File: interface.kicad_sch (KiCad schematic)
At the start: 6 parts, among them J10 RJ12, J11 Conn_01x06_Female, J8 Conn_01x06_Male, J9 RJ12, U5 MAX485E

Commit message: redone the switch connectors to accomodate a current sense print. Rearranged parts and updated silk texts to be 50% of their original size
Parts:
- renumbered C8 to C601, J8 to J601, J9 to J602, J10 to J603, J11 to J604, U5 to U601
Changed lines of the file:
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@@
   (symbol (lib_id "power:+12V") (at 143.51 50.8 0) (unit 1)
     (in_bom yes) (on_board yes) (fields_autoplaced)
-    (property "Reference" "#PWR0134" (id 0) (at 143.51 54.61 0)
+    (property "Reference" "#PWR0603" (id 0) (at 143.51 54.61 0)
       (effects (font (size 1.27 1.27)) hide)
     )
@@
   (symbol (lib_id "Connector:Conn_01x06_Female") (at 135.89 116.84 0) (mirror x) (unit 1)
     (in_bom yes) (on_board yes)
-    (property "Reference" "J11" (id 0) (at 136.6012 116.4785 0)
+    (property "Reference" "J604" (id 0) (at 136.6012 116.4785 0)
       (effects (font (size 1.27 1.27)) (justify left))
     )
@@
   (symbol (lib_id "power:GND") (at 143.51 93.98 0) (unit 1)
     (in_bom yes) (on_board yes) (fields_autoplaced)
-    (property "Reference" "#PWR0138" (id 0) (at 143.51 100.33 0)
+    (property "Reference" "#PWR0606" (id 0) (at 143.51 100.33 0)
       (effects (font (size 1.27 1.27)) hide)
     )
@@
   (symbol (lib_id "Connector:RJ12") (at 130.81 86.36 0) (unit 1)
     (in_bom yes) (on_board yes) (fields_autoplaced)
-    (property "Reference" "J10" (id 0) (at 130.81 72.5002 0))
+    (property "Reference" "J603" (id 0) (at 130.81 72.5002 0))
     (property "Value" "RJ12" (id 1) (at 130.81 75.0371 0))
     (property "Footprint" "Connector_RJ:RJ12_Amphenol_54601" (id 2) (at 130.81 85.725 90)
@@
   (symbol (lib_id "power:+12V") (at 128.27 107.95 0) (unit 1)
     (in_bom yes) (on_board yes) (fields_autoplaced)
-    (property "Reference" "#PWR0137" (id 0) (at 128.27 111.76 0)
+    (property "Reference" "#PWR0601" (id 0) (at 128.27 111.76 0)
       (effects (font (size 1.27 1.27)) hide)
     )
@@
   (symbol (lib_id "power:GND") (at 167.64 116.84 0) (unit 1)
     (in_bom yes) (on_board yes) (fields_autoplaced)
-    (property "Reference" "#PWR0140" (id 0) (at 167.64 123.19 0)
+    (property "Reference" "#PWR0610" (id 0) (at 167.64 123.19 0)
       (effects (font (size 1.27 1.27)) hide)
     )
@@
   (symbol (lib_id "Connector:Conn_01x06_Male") (at 120.65 116.84 0) (mirror x) (unit 1)
     (in_bom yes) (on_board yes)
-    (property "Reference" "J8" (id 0) (at 121.285 125.9627 0))
+    (property "Reference" "J601" (id 0) (at 121.285 125.9627 0))
     (property "Value" "Conn_01x06_Male" (id 1) (at 146.05 114.3 0))
     (property "Footprint" "Connector_PinHeader_2.54mm:PinHeader_1x06_P2.54mm_Horizontal" (id 2) (at 120.65 116.84 0)
@@
   (symbol (lib_id "Interface_UART:MAX485E") (at 162.56 67.31 0) (mirror y) (unit 1)
     (in_bom yes) (on_board yes) (fields_autoplaced)
-    (property "Reference" "U5" (id 0) (at 163.0806 53.4502 0)
+    (property "Reference" "U601" (id 0) (at 163.0806 53.4502 0)
       (effects (font (size 1.27 1.27)) (justify right))
     )
@@
   (symbol (lib_id "power:GND") (at 143.51 67.31 0) (unit 1)
     (in_bom yes) (on_board yes) (fields_autoplaced)
-    (property "Reference" "#PWR0136" (id 0) (at 143.51 73.66 0)
+    (property "Reference" "#PWR0604" (id 0) (at 143.51 73.66 0)
       (effects (font (size 1.27 1.27)) hide)
     )
@@
   (symbol (lib_id "power:+5V") (at 167.64 104.14 0) (unit 1)
     (in_bom yes) (on_board yes) (fields_autoplaced)
-    (property "Reference" "#PWR0142" (id 0) (at 167.64 107.95 0)
+    (property "Reference" "#PWR0609" (id 0) (at 167.64 107.95 0)
       (effects (font (size 1.27 1.27)) hide)
     )
@@
   (symbol (lib_id "Device:C") (at 167.64 110.49 0) (unit 1)
     (in_bom yes) (on_board yes) (fields_autoplaced)
-    (property "Reference" "C8" (id 0) (at 170.561 109.6553 0)
+    (property "Reference" "C601" (id 0) (at 170.561 109.6553 0)
       (effects (font (size 1.27 1.27)) (justify left))
     )
@@
   (symbol (lib_id "power:+5V") (at 162.56 50.8 0) (unit 1)
     (in_bom yes) (on_board yes) (fields_autoplaced)
-    (property "Reference" "#PWR0133" (id 0) (at 162.56 54.61 0)
+    (property "Reference" "#PWR0607" (id 0) (at 162.56 54.61 0)
       (effects (font (size 1.27 1.27)) hide)
     )
@@
   (symbol (lib_id "power:+12V") (at 143.51 77.47 0) (unit 1)
     (in_bom yes) (on_board yes) (fields_autoplaced)
-    (property "Reference" "#PWR0135" (id 0) (at 143.51 81.28 0)
+    (property "Reference" "#PWR0605" (id 0) (at 143.51 81.28 0)
       (effects (font (size 1.27 1.27)) hide)
     )
@@
   (symbol (lib_id "power:GND") (at 162.56 85.09 0) (unit 1)
     (in_bom yes) (on_board yes) (fields_autoplaced)
-    (property "Reference" "#PWR0143" (id 0) (at 162.56 91.44 0)
+    (property "Reference" "#PWR0608" (id 0) (at 162.56 91.44 0)
       (effects (font (size 1.27 1.27)) hide)
     )
@@
   (symbol (lib_id "power:GND") (at 128.27 123.19 0) (unit 1)
     (in_bom yes) (on_board yes) (fields_autoplaced)
-    (property "Reference" "#PWR0139" (id 0) (at 128.27 129.54 0)
+    (property "Reference" "#PWR0602" (id 0) (at 128.27 129.54 0)
       (effects (font (size 1.27 1.27)) hide)
     )
@@
   (symbol (lib_id "Connector:RJ12") (at 130.81 59.69 0) (unit 1)
     (in_bom yes) (on_board yes) (fields_autoplaced)
-    (property "Reference" "J9" (id 0) (at 130.81 45.8302 0))
+    (property "Reference" "J602" (id 0) (at 130.81 45.8302 0))
     (property "Value" "RJ12" (id 1) (at 130.81 48.3671 0))
     (property "Footprint" "Connector_RJ:RJ12_Amphenol_54601" (id 2) (at 130.81 59.055 90)

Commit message: I have a problem that I lose the links between symbols and footprints. I want to add a spst switch to connect the bus' voltage to the main power
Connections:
- net +12V renamed +12VA
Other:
- moved on the sheet: C601
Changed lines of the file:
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@@
     (stroke (width 0) (type default) (color 0 0 0 0))
   )
-  (wire (pts (xy 167.64 114.3) (xy 167.64 116.84))
+  (wire (pts (xy 190.5 72.39) (xy 190.5 74.93))
     (stroke (width 0) (type default) (color 0 0 0 0))
   )
@@
     (stroke (width 0) (type default) (color 0 0 0 0))
   )
-  (wire (pts (xy 167.64 104.14) (xy 167.64 106.68))
+  (wire (pts (xy 190.5 62.23) (xy 190.5 64.77))
     (stroke (width 0) (type default) (color 0 0 0 0))
   )
@@
     )
   )
-  (symbol (lib_id "power:+12V") (at 143.51 50.8 0) (unit 1)
-    (in_bom yes) (on_board yes) (fields_autoplaced)
-    (property "Reference" "#PWR0603" (id 0) (at 143.51 54.61 0)
-      (effects (font (size 1.27 1.27)) hide)
-    )
-    (property "Value" "+12V" (id 1) (at 143.51 47.1955 0))
-    (property "Footprint" "" (id 2) (at 143.51 50.8 0)
-      (effects (font (size 1.27 1.27)) hide)
-    )
-    (property "Datasheet" "" (id 3) (at 143.51 50.8 0)
+  (symbol (lib_id "power:+12VA") (at 128.27 107.95 0) (unit 1)
+    (in_bom yes) (on_board yes) (fields_autoplaced)
+    (property "Reference" "#PWR0601" (id 0) (at 128.27 111.76 0)
+      (effects (font (size 1.27 1.27)) hide)
+    )
+    (property "Value" "+12VA" (id 1) (at 128.27 104.3742 0))
+    (property "Footprint" "" (id 2) (at 128.27 107.95 0)
+      (effects (font (size 1.27 1.27)) hide)
+    )
+    (property "Datasheet" "" (id 3) (at 128.27 107.95 0)
       (effects (font (size 1.27 1.27)) hide)
     )
@@
     (pin "6")
   )
-  (symbol (lib_id "power:+12V") (at 128.27 107.95 0) (unit 1)
-    (in_bom yes) (on_board yes) (fields_autoplaced)
-    (property "Reference" "#PWR0601" (id 0) (at 128.27 111.76 0)
-      (effects (font (size 1.27 1.27)) hide)
-    )
-    (property "Value" "+12V" (id 1) (at 128.27 104.3742 0))
-    (property "Footprint" "" (id 2) (at 128.27 107.95 0)
-      (effects (font (size 1.27 1.27)) hide)
-    )
-    (property "Datasheet" "" (id 3) (at 128.27 107.95 0)
-      (effects (font (size 1.27 1.27)) hide)
-    )
-    (pin "1")
-  )
-  (symbol (lib_id "power:GND") (at 167.64 116.84 0) (unit 1)
-    (in_bom yes) (on_board yes) (fields_autoplaced)
-    (property "Reference" "#PWR0610" (id 0) (at 167.64 123.19 0)
-      (effects (font (size 1.27 1.27)) hide)
-    )
-    (property "Value" "GND" (id 1) (at 167.64 121.2834 0))
-    (property "Footprint" "" (id 2) (at 167.64 116.84 0)
-      (effects (font (size 1.27 1.27)) hide)
-    )
-    (property "Datasheet" "" (id 3) (at 167.64 116.84 0)
+  (symbol (lib_id "power:GND") (at 190.5 74.93 0) (unit 1)
+    (in_bom yes) (on_board yes) (fields_autoplaced)
+    (property "Reference" "#PWR0610" (id 0) (at 190.5 81.28 0)
+      (effects (font (size 1.27 1.27)) hide)
+    )
+    (property "Value" "GND" (id 1) (at 190.5 79.3734 0))
+    (property "Footprint" "" (id 2) (at 190.5 74.93 0)
+      (effects (font (size 1.27 1.27)) hide)
+    )
+    (property "Datasheet" "" (id 3) (at 190.5 74.93 0)
       (effects (font (size 1.27 1.27)) hide)
     )
@@
     (pin "1")
   )
-  (symbol (lib_id "power:+5V") (at 167.64 104.14 0) (unit 1)
-    (in_bom yes) (on_board yes) (fields_autoplaced)
-    (property "Reference" "#PWR0609" (id 0) (at 167.64 107.95 0)
-      (effects (font (size 1.27 1.27)) hide)
-    )
-    (property "Value" "+5V" (id 1) (at 167.64 100.5642 0))
-    (property "Footprint" "" (id 2) (at 167.64 104.14 0)
-      (effects (font (size 1.27 1.27)) hide)
-    )
-    (property "Datasheet" "" (id 3) (at 167.64 104.14 0)
-      (effects (font (size 1.27 1.27)) hide)
-    )
-    (pin "1")
-  )
-  (symbol (lib_id "Device:C") (at 167.64 110.49 0) (unit 1)
-    (in_bom yes) (on_board yes) (fields_autoplaced)
-    (property "Reference" "C601" (id 0) (at 170.561 109.6553 0)
+  (symbol (lib_id "power:+5V") (at 190.5 62.23 0) (unit 1)
+    (in_bom yes) (on_board yes) (fields_autoplaced)
+    (property "Reference" "#PWR0609" (id 0) (at 190.5 66.04 0)
+      (effects (font (size 1.27 1.27)) hide)
+    )
+    (property "Value" "+5V" (id 1) (at 190.5 58.6542 0))
+    (property "Footprint" "" (id 2) (at 190.5 62.23 0)
+      (effects (font (size 1.27 1.27)) hide)
+    )
+    (property "Datasheet" "" (id 3) (at 190.5 62.23 0)
+      (effects (font (size 1.27 1.27)) hide)
+    )
+    (pin "1")
+  )
+  (symbol (lib_id "Device:C") (at 190.5 68.58 0) (unit 1)
+    (in_bom yes) (on_board yes) (fields_autoplaced)
+    (property "Reference" "C601" (id 0) (at 193.421 67.7453 0)
       (effects (font (size 1.27 1.27)) (justify left))
     )
-    (property "Value" "100nF" (id 1) (at 170.561 112.1922 0)
+    (property "Value" "100nF" (id 1) (at 193.421 70.2822 0)
       (effects (font (size 1.27 1.27)) (justify left))
     )
-    (property "Footprint" "Capacitor_THT:C_Disc_D3.0mm_W1.6mm_P2.50mm" (id 2) (at 168.6052 114.3 0)
-      (effects (font (size 1.27 1.27)) hide)
-    )
-    (property "Datasheet" "~" (id 3) (at 167.64 110.49 0)
+    (property "Footprint" "Capacitor_THT:C_Disc_D3.0mm_W1.6mm_P2.50mm" (id 2) (at 191.4652 72.39 0)
+      (effects (font (size 1.27 1.27)) hide)
+    )
+    (property "Datasheet" "~" (id 3) (at 190.5 68.58 0)
       (effects (font (size 1.27 1.27)) hide)
     )
@@
     (pin "1")
   )
-  (symbol (lib_id "power:+12V") (at 143.51 77.47 0) (unit 1)
+  (symbol (lib_id "power:+12VA") (at 143.51 77.47 0) (unit 1)
     (in_bom yes) (on_board yes) (fields_autoplaced)
     (property "Reference" "#PWR0605" (id 0) (at 143.51 81.28 0)
       (effects (font (size 1.27 1.27)) hide)
     )
-    (property "Value" "+12V" (id 1) (at 143.51 73.8655 0))
+    (property "Value" "+12VA" (id 1) (at 143.51 73.8942 0))
     (property "Footprint" "" (id 2) (at 143.51 77.47 0)
       (effects (font (size 1.27 1.27)) hide)
@@
       (effects (font (size 1.27 1.27)) hide)
     )
+    (pin "1")
+  )
+  (symbol (lib_id "power:+12VA") (at 143.51 50.8 0) (unit 1)
+    (in_bom yes) (on_board yes) (fields_autoplaced)
+    (property "Reference" "#PWR0603" (id 0) (at 143.51 54.61 0)
+      (effects (font (size 1.27 1.27)) hide)
+    )
+    (property "Value" "" (id 1) (at 143.51 47.2242 0))
+    (property "Footprint" "" (id 2) (at 143.51 50.8 0)
+      (effects (font (size 1.27 1.27)) hide)
+    )
+    (property "Datasheet" "" (id 3) (at 143.51 50.8 0)
+      (effects (font (size 1.27 1.27)) hide)
+    )

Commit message: added something to debug the channel buttons
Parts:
- C601: footprint Capacitor_THT:C_Disc_D3.0mm_W1.6mm_P2.50mm -> Capacitor_SMD:C_0805_2012Metric
- U601: footprint Package_DIP:DIP-8_W7.62mm_Socket -> Package_SO:SOIC-8_3.9x4.9mm_P1.27mm
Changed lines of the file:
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@@
       (effects (font (size 1.27 1.27)) (justify right))
     )
-    (property "Footprint" "Package_DIP:DIP-8_W7.62mm_Socket" (id 2) (at 162.56 85.09 0)
+    (property "Footprint" "Package_SO:SOIC-8_3.9x4.9mm_P1.27mm" (id 2) (at 162.56 85.09 0)
       (effects (font (size 1.27 1.27)) hide)
     )
@@
       (effects (font (size 1.27 1.27)) (justify left))
     )
-    (property "Footprint" "Capacitor_THT:C_Disc_D3.0mm_W1.6mm_P2.50mm" (id 2) (at 191.4652 72.39 0)
+    (property "Footprint" "Capacitor_SMD:C_0805_2012Metric" (id 2) (at 191.4652 72.39 0)
       (effects (font (size 1.27 1.27)) hide)
     )
@@
       (effects (font (size 1.27 1.27)) hide)
     )
-    (property "Value" "" (id 1) (at 143.51 47.2242 0))
+    (property "Value" "+12VA" (id 1) (at 143.51 47.2242 0))
     (property "Footprint" "" (id 2) (at 143.51 50.8 0)
       (effects (font (size 1.27 1.27)) hide)

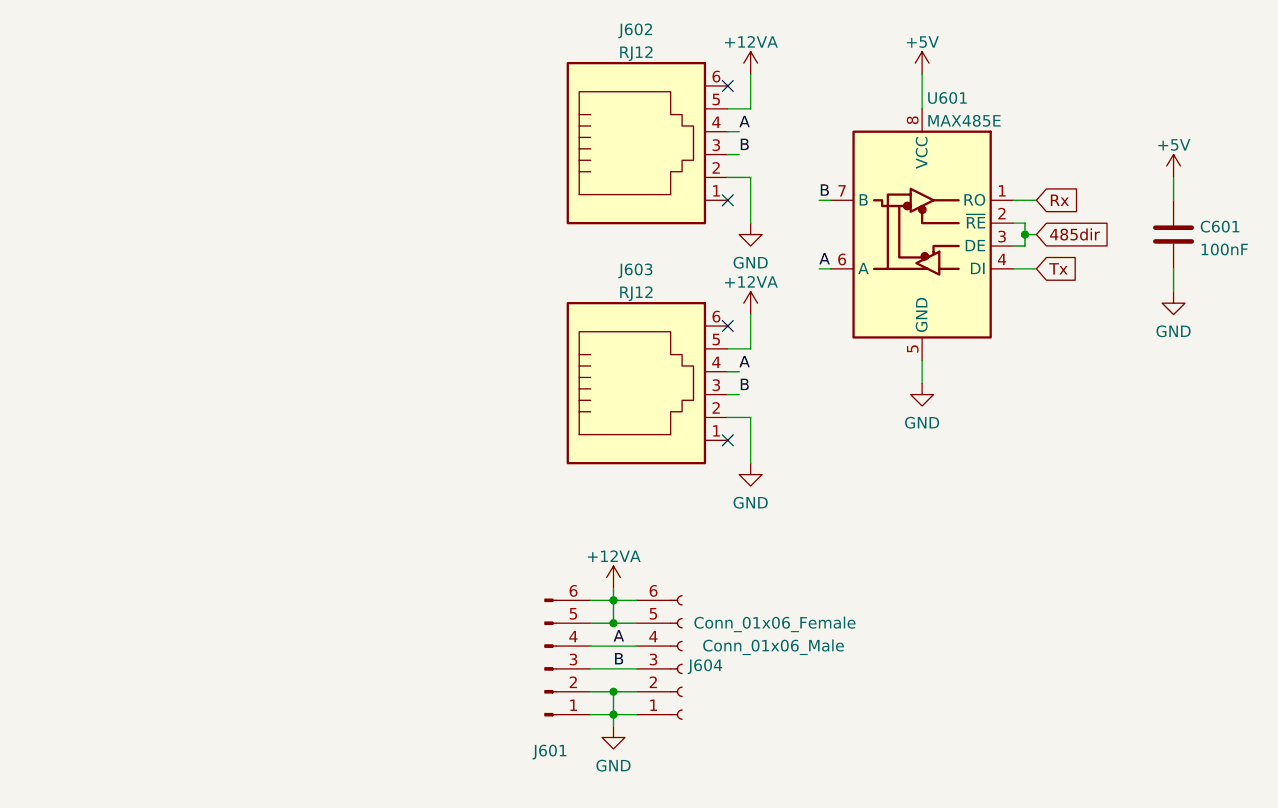
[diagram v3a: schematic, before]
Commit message: redid this project. I want to use an atmega328 so I ditched some IO. I retained 4 servo, 1 H-bridge (should make it double), 3 relays, 6 GPIO, 1 potentiometer and loconet interface. And I still have a config button
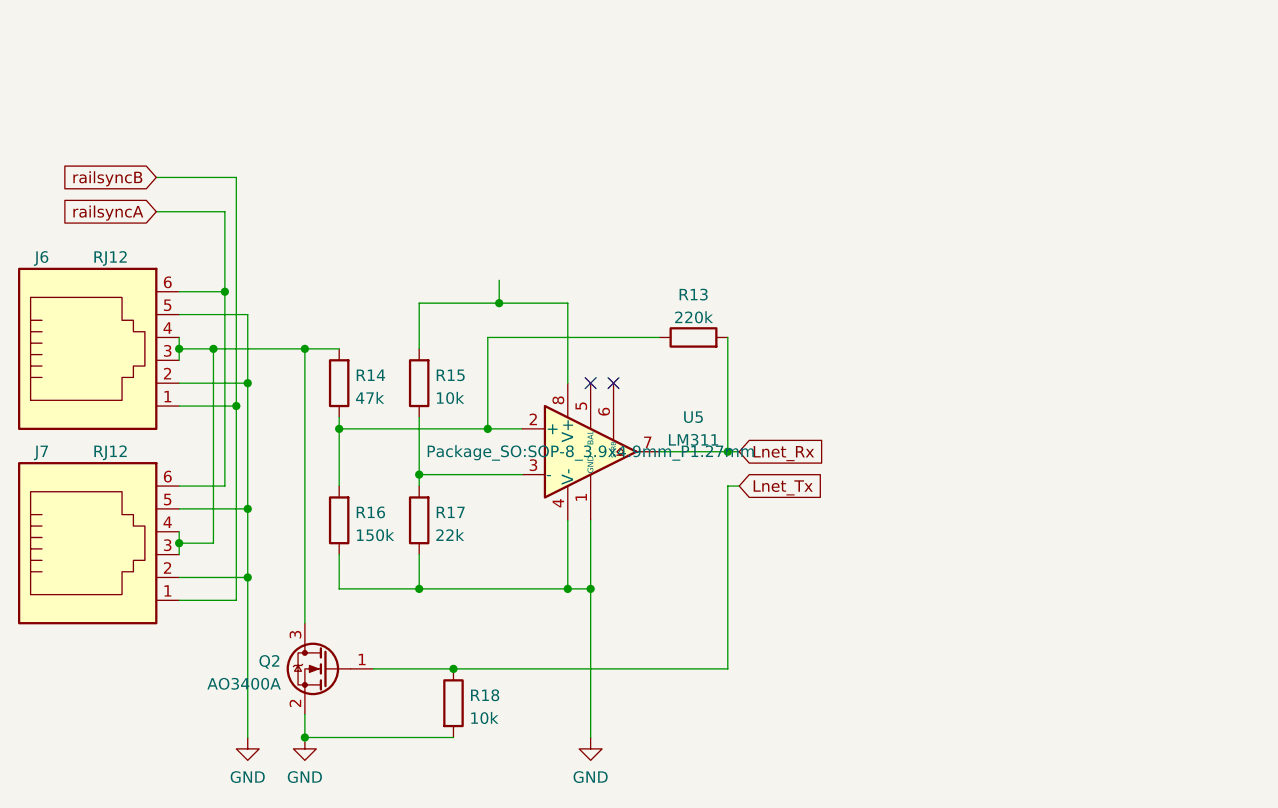
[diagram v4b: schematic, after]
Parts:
- removed C601: 100nF, Capacitor_SMD:C_0805_2012Metric, symbol Device:C
- removed J601: Conn_01x06_Male, Connector_PinHeader_2.54mm:PinHeader_1x06_P2.54mm_Horizontal, symbol Connector:Conn_01x06_Male
- removed J602, J603: RJ12, Connector_RJ:RJ12_Amphenol_54601, symbol Connector:RJ12
- removed J604: Conn_01x06_Female, Connector_PinSocket_2.54mm:PinSocket_1x06_P2.54mm_Horizontal, symbol Connector:Conn_01x06_Female
- removed U601: MAX485E, Package_SO:SOIC-8_3.9x4.9mm_P1.27mm, symbol Interface_UART:MAX485E
- added J6, J7: RJ12, Connector_RJ:RJ25_Wayconn_MJEA-660X1_Horizontal, symbol Connector:RJ12
- added Q2: AO3400A, Package_TO_SOT_SMD:SOT-23, symbol Transistor_FET:AO3400A
- added R13: 220k, Resistor_SMD:R_0805_2012Metric_Pad1.20x1.40mm_HandSolder, symbol Device:R
- added R14: 47k, Resistor_SMD:R_0805_2012Metric_Pad1.20x1.40mm_HandSolder, symbol Device:R
- added R15, R18: 10k, Resistor_SMD:R_0805_2012Metric_Pad1.20x1.40mm_HandSolder, symbol Device:R
- added R16: 150k, Resistor_SMD:R_0805_2012Metric_Pad1.20x1.40mm_HandSolder, symbol Device:R
- added R17: 22k, Resistor_SMD:R_0805_2012Metric_Pad1.20x1.40mm_HandSolder, symbol Device:R
- added U5: LM311, Package_SO:SOP-8_3.9x4.9mm_P1.27mm, symbol Comparator:LM311
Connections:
- net GND: now also J6.2, J6.5, J7.2, J7.5, Q2.2 (S), R16.1, R17.1, R18.2, U5.1 (GND), U5.4 (V-)
- new net: R13.1, R14.1, R16.2, U5.2 (+)
- new net: R15.1, R17.2, U5.3 (-)
- new net: R15.2, U5.8 (V+)
- new net: J6.3, J6.4, J7.3, J7.4, Q2.3 (D), R14.2
- new net Lnet_Rx: R13.2, U5.7
- new net Lnet_Tx: Q2.1 (G), R18.1
- new net railsyncA: J6.6, J7.6
- new net railsyncB: J6.1, J7.1
- no-connect marks 4 -> 2
